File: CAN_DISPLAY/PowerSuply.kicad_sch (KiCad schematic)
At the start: 27 parts, among them J10 DCDC 5V 3A, J6 12V, J8 DCDC 5V, U4 AMS1117-3.3

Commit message: PCB Fixes
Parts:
- removed D1: 1N4007, Diode_THT:D_DO-41_SOD81_P10.16mm_Horizontal, symbol Diode:1N4007
- added D12: 1N5822, Diode_THT:D_DO-201AD_P15.24mm_Horizontal, symbol Diode:1N5822
- C10: value 10u -> 47u; footprint Capacitor_SMD:CP_Elec_6.3x4.5 -> Capacitor_SMD:CP_Elec_5x5.8
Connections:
- net at C5.1, FL1.1, JP1.2 (B): now also D12.1 (K)
- net at F1.2: now also D12.2 (A)
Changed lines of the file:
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@@
-    )
-  )
-  (symbol (lib_id "Diode:1N4007") (at 34.29 66.04 180) (unit 1)
-    (in_bom yes) (on_board yes) (dnp no)
-    (property "Reference" "D1" (at 34.29 59.69 0)
-      (effects (font (size 1.27 1.27)))
-    )
-    (property "Value" "1N4007" (at 34.29 62.23 0)
-      (effects (font (size 1.27 1.27)))
-    )
-    (property "Footprint" "Diode_THT:D_DO-41_SOD81_P10.16mm_Horizontal" (at 34.29 61.595 0)
-      (effects (font (size 1.27 1.27)) hide)
-    )
-    (property "Datasheet" "http://www.vishay.com/docs/88503/1n4001.pdf" (at 34.29 66.04 0)
-      (effects (font (size 1.27 1.27)) hide)
-    )
-    (property "Sim.Device" "D" (at 34.29 66.04 0)
-      (effects (font (size 1.27 1.27)) hide)
-    )
-    (property "Sim.Pins" "1=K 2=A" (at 34.29 66.04 0)
-      (effects (font (size 1.27 1.27)) hide)
-    )
-    (pin "1")
-    (pin "2")
-    (instances
-      (project "CAN_DISPLAY"
-        (path "/7b7bcc60-3b35-483b-8f75-db7ec854d7bb/0efeef53-f612-43e6-99d4-b53087b36e31"
-          (reference "D1") (unit 1)
-        )
-        (path "/7b7bcc60-3b35-483b-8f75-db7ec854d7bb/64058649-9106-47b8-8357-4a2d690c60fd"
-          (reference "D6") (unit 1)
-        )
-      )
     )
   )
@@
     )
   )
+  (symbol (lib_id "Diode:1N5822") (at 34.29 66.04 180) (unit 1)
+    (in_bom yes) (on_board yes) (dnp no) (fields_autoplaced)
+    (property "Reference" "D12" (at 34.6075 59.69 0)
+      (effects (font (size 1.27 1.27)))
+    )
+    (property "Value" "1N5822" (at 34.6075 62.23 0)
+      (effects (font (size 1.27 1.27)))
+    )
+    (property "Footprint" "Diode_THT:D_DO-201AD_P15.24mm_Horizontal" (at 34.29 61.595 0)
+      (effects (font (size 1.27 1.27)) hide)
+    )
+    (property "Datasheet" "http://www.vishay.com/docs/88526/1n5820.pdf" (at 34.29 66.04 0)
+      (effects (font (size 1.27 1.27)) hide)
+    )
+    (pin "1")
+    (pin "2")
+    (instances
+      (project "CAN_DISPLAY"
+        (path "/7b7bcc60-3b35-483b-8f75-db7ec854d7bb/64058649-9106-47b8-8357-4a2d690c60fd"
+          (reference "D12") (unit 1)
+        )
+      )
+    )
+  )
   (symbol (lib_id "Device:C_Small") (at 45.085 144.145 0) (unit 1)
     (in_bom yes) (on_board yes) (dnp no)
@@
       (effects (font (size 1.27 1.27)) (justify left))
     )
-    (property "Value" "10u" (at 138.43 140.335 0)
-      (effects (font (size 1.27 1.27)) (justify left))
-    )
-    (property "Footprint" "Capacitor_SMD:CP_Elec_6.3x4.5" (at 135.89 137.795 0)
-      (effects (font (size 1.27 1.27)) hide)
-    )
+    (property "Value" "47u" (at 138.43 140.335 0)
+      (effects (font (size 1.27 1.27)) (justify left))
+    )
+    (property "Footprint" "Capacitor_SMD:CP_Elec_5x5.8" (at 135.89 137.795 0)
+      (effects (font (size 1.27 1.27)) hide)
+    )

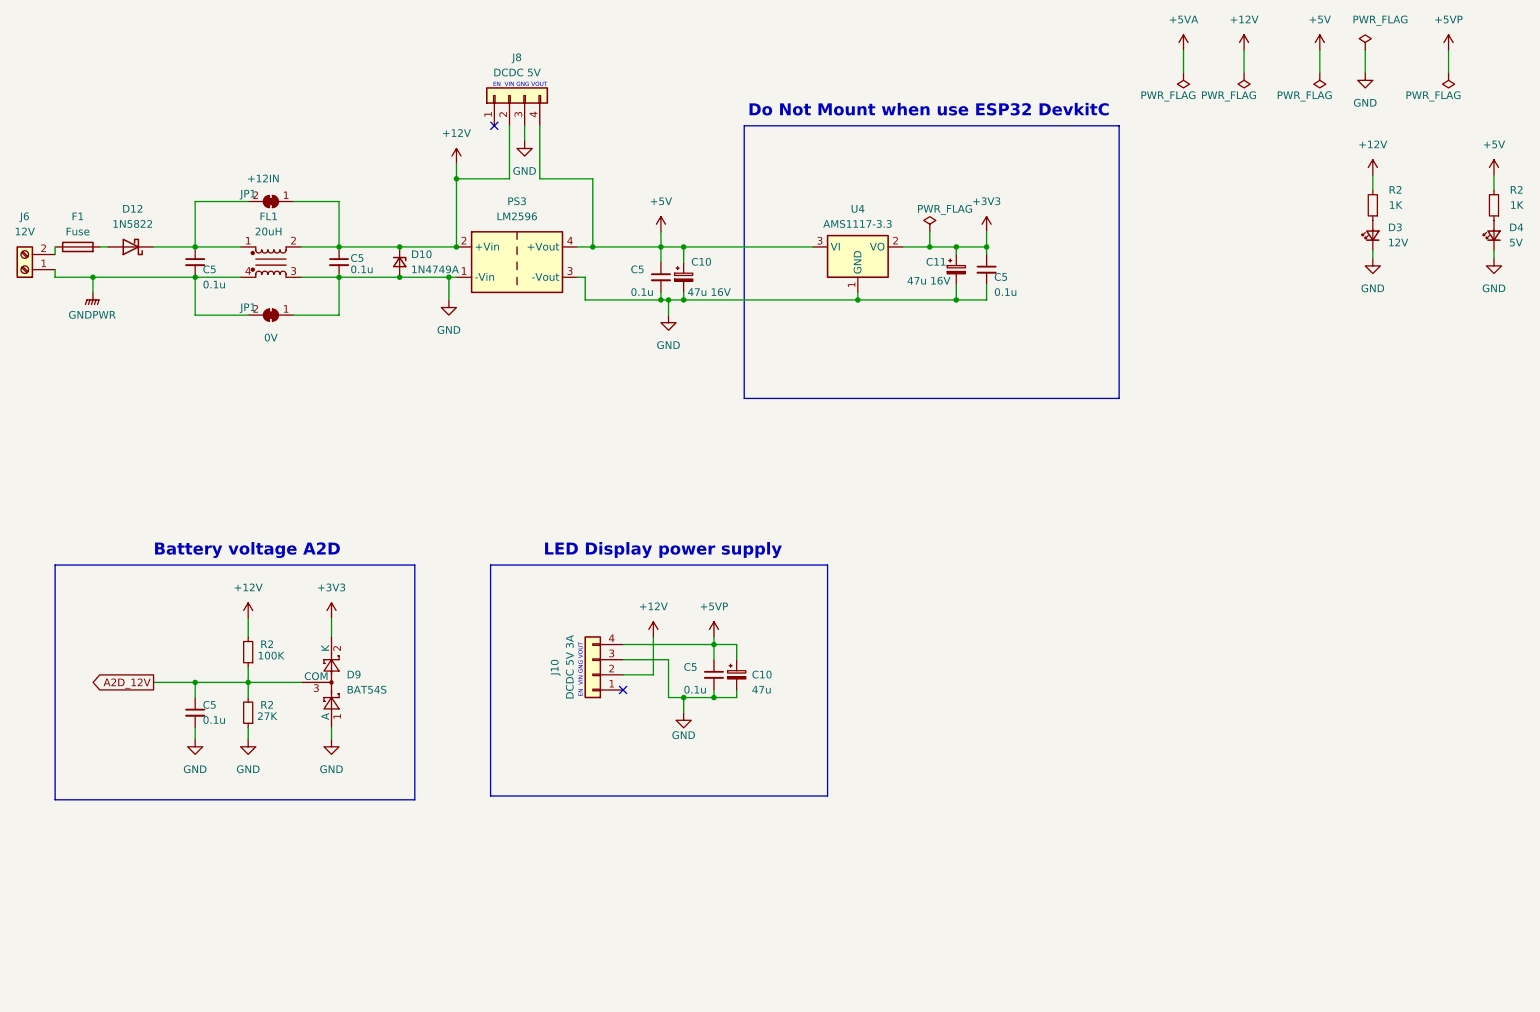
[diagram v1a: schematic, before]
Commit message: Add Ambient Light
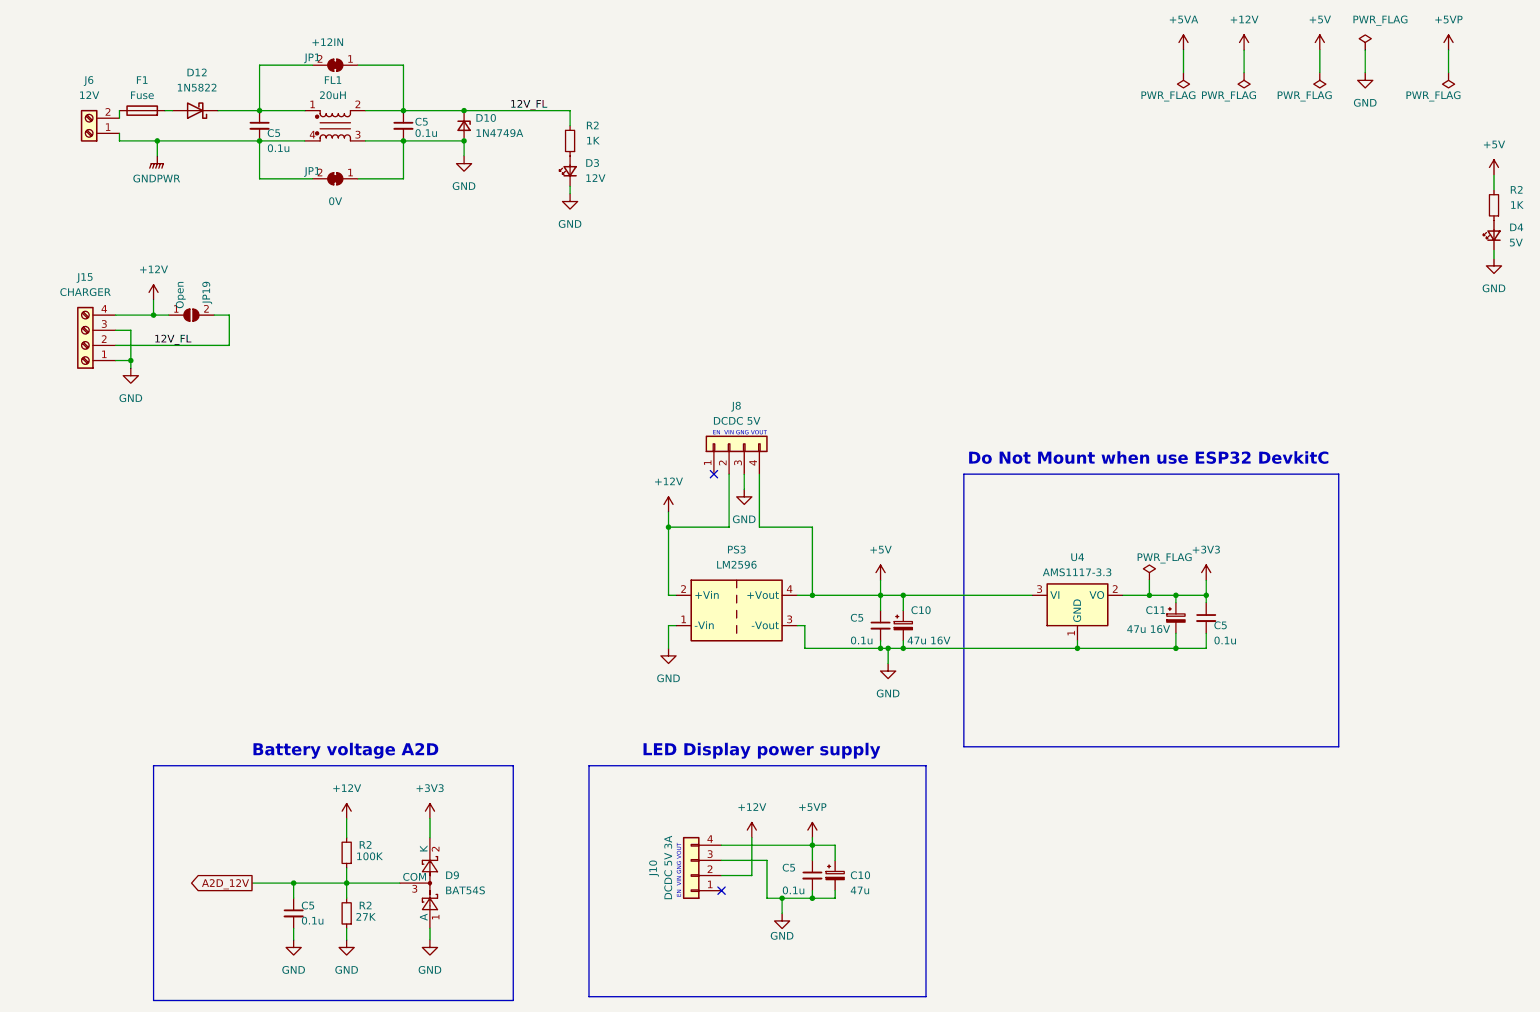
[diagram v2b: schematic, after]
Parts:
- added J15: CHARGER, TerminalBlock:TerminalBlock_bornier-4_P5.08mm, symbol Connector:Screw_Terminal_01x04
- added JP19: Open, Jumper:SolderJumper-2_P1.3mm_Open_RoundedPad1.0x1.5mm, symbol Jumper:SolderJumper_2_Open
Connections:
- net +12V: now also J15.4 (Pin_4), JP19.1 (A); no longer C5.1, D10.1 (K), FL1.2, JP1.1 (A), R2.2
- net GND: now also J15.1 (Pin_1), J15.3 (Pin_3)
- new net 12V_FL: C5.1, D10.1 (K), FL1.2, J15.2 (Pin_2), JP1.1 (A), JP19.2 (B), R2.2
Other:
- moved on the sheet: C10, C11, C5, D10, D12, D3, D9, F1, FL1, J10, J6, J8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

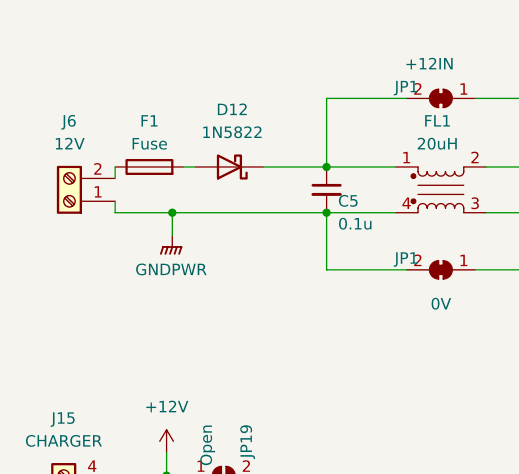
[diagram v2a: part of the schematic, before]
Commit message: Added Light Sensor
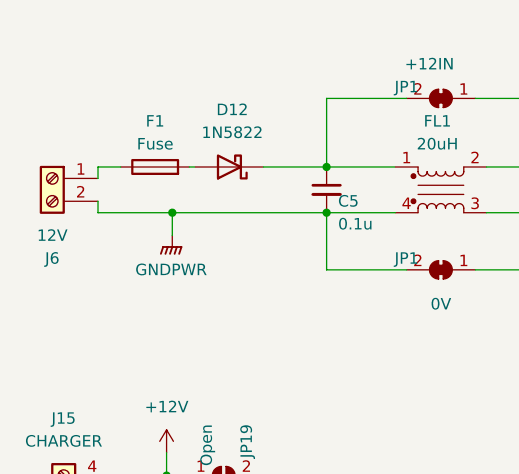
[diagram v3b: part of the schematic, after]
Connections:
- net GNDPWR: now also J6.2 (Pin_2); no longer J6.1 (Pin_1)
- net at F1.1: now also J6.1 (Pin_1); no longer J6.2 (Pin_2)
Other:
- moved on the sheet: F1, J6
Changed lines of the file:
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@@
+    (stroke (width 0) (type default))
+  )
+  (wire (pts (xy 30.48 43.18) (xy 30.48 44.45))
     (stroke (width 0) (type default))
   )
@@
     (stroke (width 0) (type default))
   )
+  (wire (pts (xy 33.02 43.18) (xy 30.48 43.18))
+    (stroke (width 0) (type default))
+  )
   (wire (pts (xy 134.62 104.14) (xy 134.62 113.03))
     (stroke (width 0) (type default))
@@
     (stroke (width 0) (type default))
   )
+  (wire (pts (xy 30.48 48.26) (xy 30.48 46.99))
+    (stroke (width 0) (type default))
+  )
   (wire (pts (xy 214.63 121.92) (xy 214.63 124.46))
     (stroke (width 0) (type default))
@@
     (stroke (width 0) (type default))
   )
-  (wire (pts (xy 32.385 43.18) (xy 32.385 44.45))
-    (stroke (width 0) (type default))
-  )
   (wire (pts (xy 90.17 48.26) (xy 90.17 50.8))
     (stroke (width 0) (type default))
@@
     (stroke (width 0) (type default))
   )
-  (wire (pts (xy 38.735 48.26) (xy 32.385 48.26))
-    (stroke (width 0) (type default))
-  )
   (wire (pts (xy 31.75 77.47) (xy 38.1 77.47))
     (stroke (width 0) (type default))
@@
     (stroke (width 0) (type default))
   )
+  (wire (pts (xy 30.48 48.26) (xy 38.735 48.26))
+    (stroke (width 0) (type default))
+  )
   (wire (pts (xy 163.83 132.08) (xy 163.83 133.35))
     (stroke (width 0) (type default))
@@
     (stroke (width 0) (type default))
   )
-  (wire (pts (xy 40.005 43.18) (xy 41.275 43.18))
+  (wire (pts (xy 40.64 43.18) (xy 41.275 43.18))
     (stroke (width 0) (type default))
   )
@@
   )
   (wire (pts (xy 72.39 35.56) (xy 80.01 35.56))
-    (stroke (width 0) (type default))
-  )
-  (wire (pts (xy 32.385 48.26) (xy 32.385 46.99))
     (stroke (width 0) (type default))
   )
@@
     )
   )
-  (symbol (lib_id "Device:Fuse") (at 36.195 43.18 90) (unit 1)
-    (in_bom yes) (on_board yes) (dnp no) (fields_autoplaced)
-    (property "Reference" "F1" (at 36.195 38.1 90)
-      (effects (font (size 1.27 1.27)))
-    )
-    (property "Value" "Fuse" (at 36.195 40.64 90)
-      (effects (font (size 1.27 1.27)))
-    )
-    (property "Footprint" "Fuse:Fuse_Blade_Mini_directSolder" (at 36.195 44.958 90)
-      (effects (font (size 1.27 1.27)) hide)
-    )
-    (property "Datasheet" "~" (at 36.195 43.18 0)
+  (symbol (lib_id "Device:Fuse") (at 36.83 43.18 90) (unit 1)
+    (in_bom yes) (on_board yes) (dnp no) (fields_autoplaced)
+    (property "Reference" "F1" (at 36.83 38.1 90)
+      (effects (font (size 1.27 1.27)))
+    )
+    (property "Value" "Fuse" (at 36.83 40.64 90)
+      (effects (font (size 1.27 1.27)))
+    )
+    (property "Footprint" "Fuse:Fuse_Blade_Mini_directSolder" (at 36.83 44.958 90)
+      (effects (font (size 1.27 1.27)) hide)
+    )
+    (property "Datasheet" "~" (at 36.83 43.18 0)
       (effects (font (size 1.27 1.27)) hide)
     )
@@
     )
   )
-  (symbol (lib_id "Connector:Screw_Terminal_01x02") (at 27.305 46.99 180) (unit 1)
-    (in_bom yes) (on_board yes) (dnp no) (fields_autoplaced)
-    (property "Reference" "J6" (at 27.305 38.1 0)
-      (effects (font (size 1.27 1.27)))
-    )
-    (property "Value" "12V" (at 27.305 40.64 0)
-      (effects (font (size 1.27 1.27)))
-    )
-    (property "Footprint" "TerminalBlock:TerminalBlock_bornier-2_P5.08mm" (at 27.305 46.99 0)
-      (effects (font (size 1.27 1.27)) hide)
-    )
-    (property "Datasheet" "~" (at 27.305 46.99 0)
-      (effects (font (size 1.27 1.27)) hide)
-    )
+  (symbol (lib_id "Connector:Screw_Terminal_01x02") (at 25.4 44.45 0) (mirror y) (unit 1)
+    (in_bom yes) (on_board yes) (dnp no)
+    (property "Reference" "J6" (at 25.4 53.34 0)
+      (effects (font (size 1.27 1.27)))
+    )
+    (property "Value" "12V" (at 25.4 50.8 0)
+      (effects (font (size 1.27 1.27)))
+    )
+    (property "Footprint" "TerminalBlock:TerminalBlock_bornier-2_P5.08mm" (at 25.4 44.45 0)
+      (effects (font (size 1.27 1.27)) hide)
+    )
+    (property "Datasheet" "~" (at 25.4 44.45 0)
+      (effects (font (size 1.27 1.27)) hide)
+    )
